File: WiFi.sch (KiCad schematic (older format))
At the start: 17 parts, among them J4 USB_B_Micro, J5 ESP_01, Q2 Q_NPN_EBC, Q3 Q_NPN_EBC, U8 CP2102N-A01-GQFN28, U9 TS5A3167DBVR

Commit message: Minor changes in pinout and layout
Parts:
- U8: symbol Interface_USB:CP2102N-A01-GQFN28 -> synermycha-electronics-rescue:CP2102N-A01-GQFN28-Interface_USB
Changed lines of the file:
@@
 $EndComp
 $Comp
-L Interface_USB:CP2102N-A01-GQFN28 U8
+L synermycha-electronics-rescue:CP2102N-A01-GQFN28-Interface_USB U8
 U 1 1 5E702C74
 P 4300 5200

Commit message: Minor update in pin connections
Connected Mouse eye led to PWM output
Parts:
- removed Q2, Q3: Q_NPN_EBC, Package_TO_SOT_SMD:SOT-23, symbol Device:Q_NPN_EBC
- added Q2, Q3: BC847, Package_TO_SOT_SMD:SOT-23, symbol Transistor_BJT:BC847
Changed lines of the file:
@@
-$EndComp
-$Comp
-L Device:Q_NPN_EBC Q2
-U 1 1 5E70ECD5
-P 5550 4500
-AR Path="/5E5F55AD/5E70ECD5" Ref="Q2"  Part="1"
-AR Path="/5E79B5DD/5E70ECD5" Ref="Q?"  Part="1"
-F 0 "Q2" V 5400 4700 50  0000 C CNN
-F 1 "Q_NPN_EBC" V 5500 4850 50  0000 C CNN
-F 2 "Package_TO_SOT_SMD:SOT-23" H 5750 4600 50  0001 C CNN
-F 3 "~" H 5550 4500 50  0001 C CNN
-	1    5550 4500
-	0    1    1    0
-$EndComp
-$Comp
-L Device:Q_NPN_EBC Q3
-U 1 1 5E70FFDF
-P 5550 4850
-AR Path="/5E5F55AD/5E70FFDF" Ref="Q3"  Part="1"
-AR Path="/5E79B5DD/5E70FFDF" Ref="Q?"  Part="1"
-F 0 "Q3" V 5500 5050 50  0000 C CNN
-F 1 "Q_NPN_EBC" V 5400 5200 50  0000 C CNN
-F 2 "Package_TO_SOT_SMD:SOT-23" H 5750 4950 50  0001 C CNN
-F 3 "~" H 5550 4850 50  0001 C CNN
-	1    5550 4850
-	0    1    -1   0
 $EndComp
 $Comp
@@
 	8350 4500 8050 4500
 Connection ~ 8050 4500
+$Comp
+L Transistor_BJT:BC847 Q2
+U 1 1 5E7F7A4F
+P 5550 4500
+F 0 "Q2" V 5450 4700 50  0000 C CNN
+F 1 "BC847" V 5550 4750 50  0000 C CNN
+F 2 "Package_TO_SOT_SMD:SOT-23" H 5750 4425 50  0001 L CIN
+F 3 "http://www.infineon.com/dgdl/Infineon-BC847SERIES_BC848SERIES_BC849SERIES_BC850SERIES-DS-v01_01-en.pdf?fileId=db3a304314dca389011541d4630a1657" H 5550 4500 50  0001 L CNN
+	1    5550 4500
+	0    1    1    0
+$EndComp
+$Comp
+L Transistor_BJT:BC847 Q3
+U 1 1 5E7F94B2
+P 5550 4850
+F 0 "Q3" V 5500 5050 50  0000 C CNN
+F 1 "BC847" V 5400 5100 50  0000 C CNN
+F 2 "Package_TO_SOT_SMD:SOT-23" H 5750 4775 50  0001 L CIN
+F 3 "http://www.infineon.com/dgdl/Infineon-BC847SERIES_BC848SERIES_BC849SERIES_BC850SERIES-DS-v01_01-en.pdf?fileId=db3a304314dca389011541d4630a1657" H 5550 4850 50  0001 L CNN
+	1    5550 4850
+	0    1    -1   0
+$EndComp
 $EndSCHEMATC

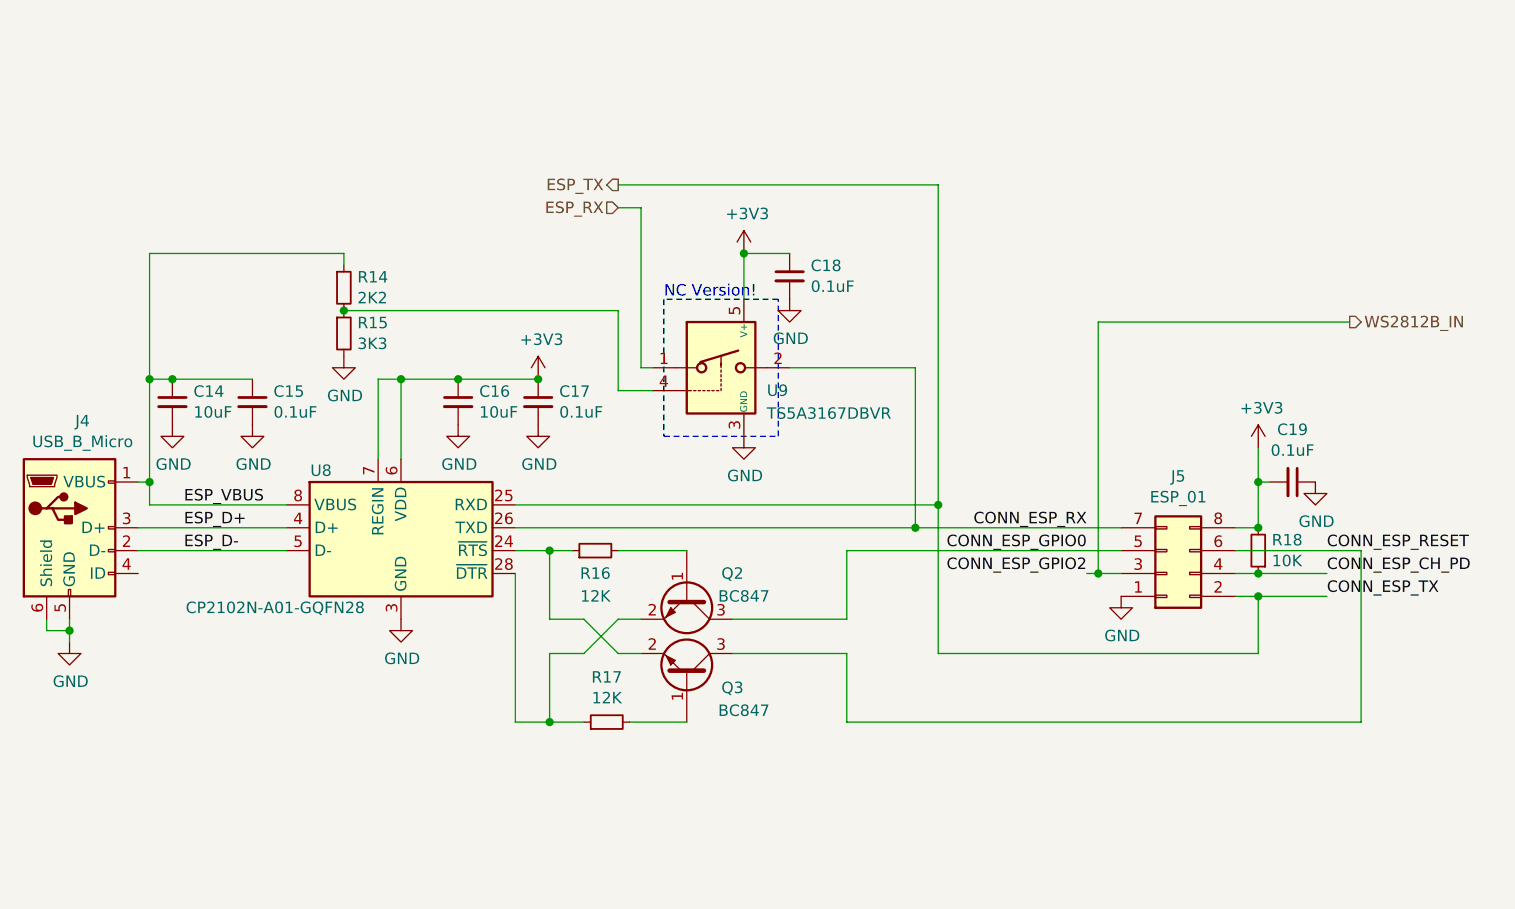
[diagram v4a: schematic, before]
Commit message: Czyszczenie
Usunięto linie 5V oraz 2V8. Poprawiono symbol dla diody RGB
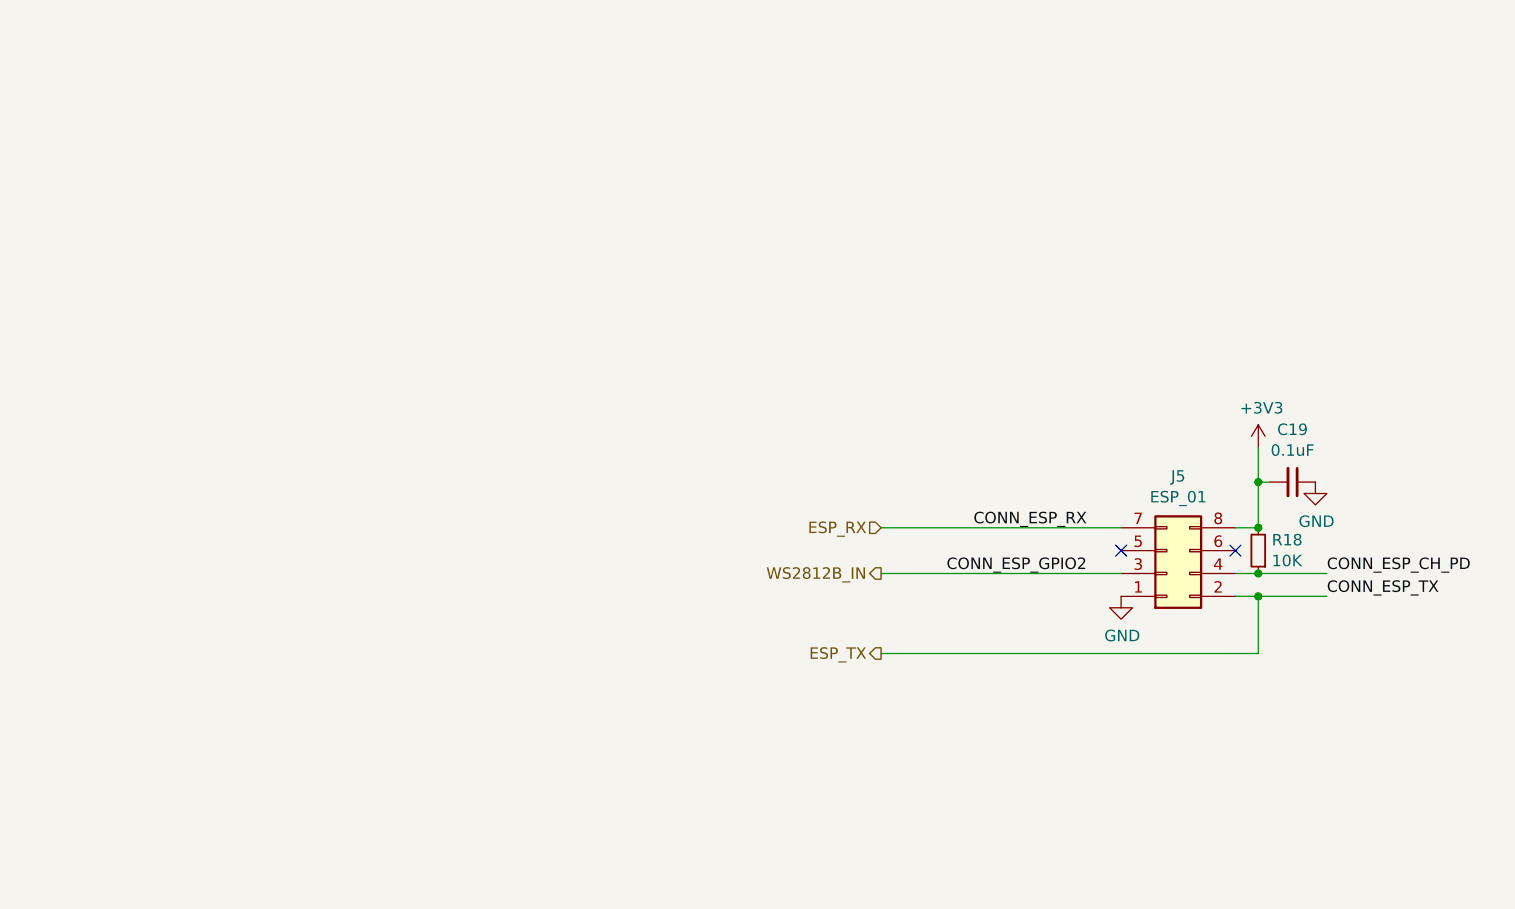
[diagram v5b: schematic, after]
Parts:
- removed C14, C16: 10uF, Capacitor_SMD:C_0603_1608Metric, symbol Device:C_Small
- removed C15, C17, C18: 0.1uF, Capacitor_SMD:C_0402_1005Metric, symbol Device:C_Small
- removed J4: USB_B_Micro, Connector_USB:USB_Micro-B_Amphenol_10103594-0001LF_Horizontal, symbol Connector:USB_B_Micro
- removed Q2, Q3: BC847, Package_TO_SOT_SMD:SOT-23, symbol Transistor_BJT:BC847
- removed R14: 2K2, Resistor_SMD:R_0402_1005Metric, symbol Device:R_Small
- removed R15: 3K3, Resistor_SMD:R_0402_1005Metric, symbol Device:R_Small
- removed R16, R17: 12K, Resistor_SMD:R_0402_1005Metric, symbol Device:R_Small
- removed U8: CP2102N-A01-GQFN28, Package_DFN_QFN:QFN-28-1EP_5x5mm_P0.5mm_EP3.35x3.35mm, symbol synermycha-electronics-rescue:CP2102N-A01-GQFN28-Interface_USB
- removed U9: TS5A3167DBVR, Package_TO_SOT_SMD:SOT-23-5, symbol Analog_Switch:TS5A3166DBVR
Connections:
- net CONN_ESP_RX is gone; now on net ESP_RX: J5.7 (Pin_7)
- net CONN_ESP_GPIO0: no longer names the net of J5.5 (Pin_5)
- net CONN_ESP_RESET: no longer names the net of J5.6 (Pin_6)
- no-connect marks 0 -> 2
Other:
- note removed: "NC Version!"

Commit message: Zmieniono moduł wifi na bluetooth oraz złącze usb - c
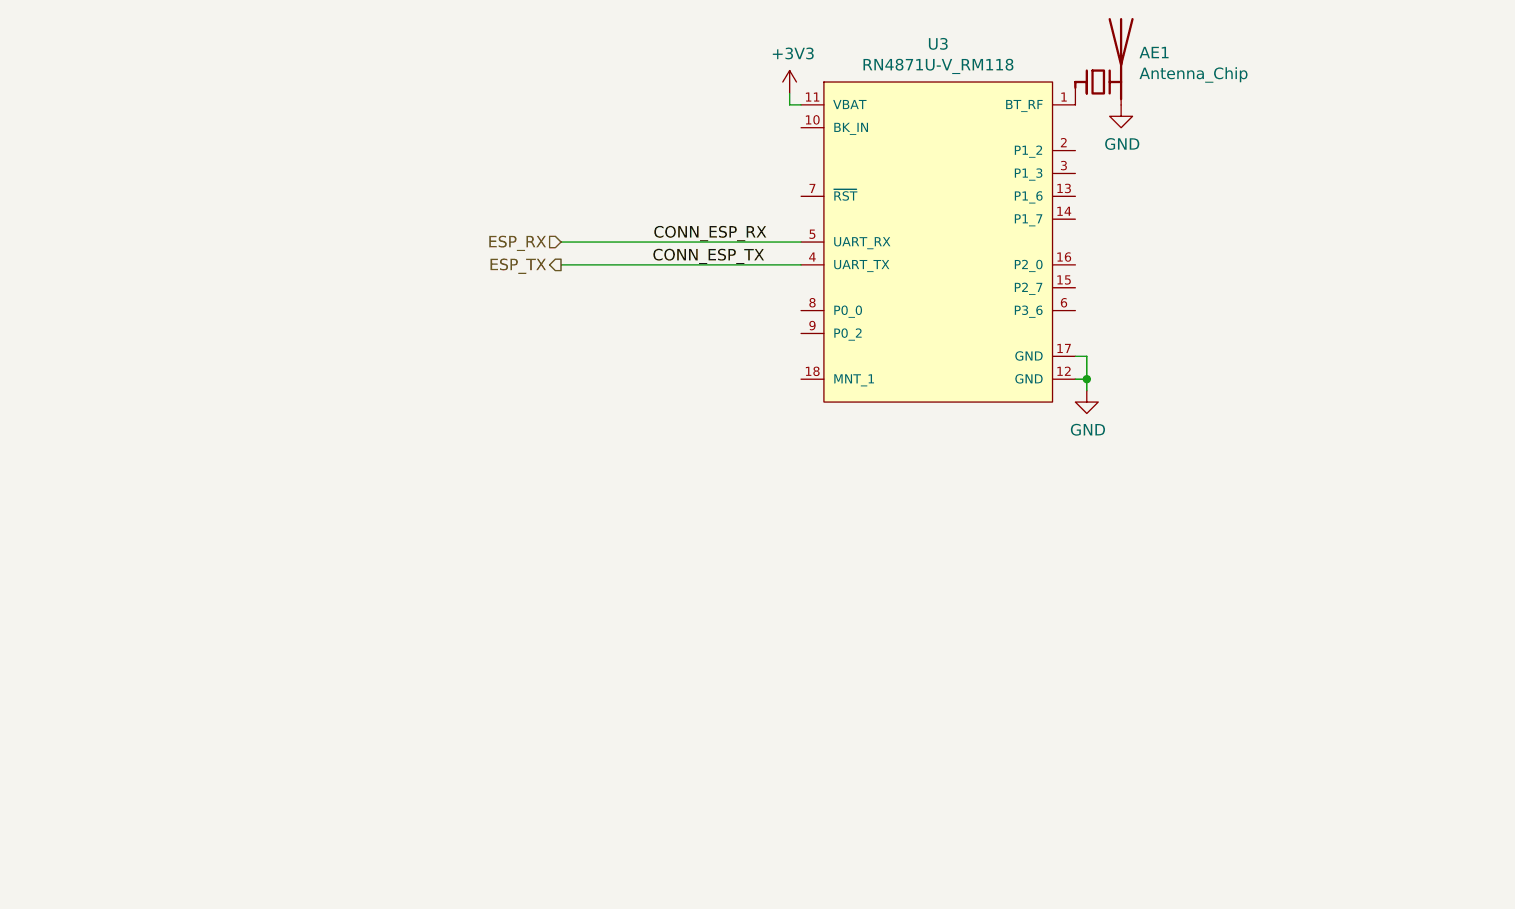
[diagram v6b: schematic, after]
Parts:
- removed C19: 0.1uF, Capacitor_SMD:C_0402_1005Metric, symbol Device:C_Small
- removed J5: ESP_01, Connector_PinSocket_2.54mm:PinSocket_2x04_P2.54mm_Vertical_SMD, symbol Connector_Generic:Conn_02x04_Odd_Even
- removed R18: 10K, Resistor_SMD:R_0402_1005Metric, symbol Device:R_Small
- added AE1: Antenna_Chip, RF_Antenna:Johanson_2450AT18x100, symbol Device:Antenna_Chip
- added U3: RN4871U-V_RM118, eec:Microchip-RN4871U-V_RM118-0, symbol eec:RN4871U-V_RM118
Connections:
- net +3V3: now also U3.11 (VBAT)
- net ESP_RX: now also U3.5 (UART_RX)
- net ESP_TX: now also U3.4 (UART_TX)
- net GND: now also AE1.2 (PCB_Trace), U3.12 (GND), U3.17 (GND)
- new net: AE1.1 (FEED), U3.1 (BT_RF)
- no-connect marks 2 -> 0
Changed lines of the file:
@@
 Comment4 ""
 $EndDescr
-Text HLabel 6400 4200 0    50   Input ~ 0
+Text HLabel 5000 2950 0    50   Input ~ 0
 ESP_RX
-Text HLabel 6400 4750 0    50   Output ~ 0
+Text HLabel 5000 3050 0    50   Output ~ 0
 ESP_TX
-Text HLabel 6400 4400 0    50   Output ~ 0
-WS2812B_IN
-Wire Wire Line
-	8050 4000 8050 4200
-Connection ~ 8050 4000
-Wire Wire Line
-	8100 4000 8050 4000
-Wire Wire Line
-	8050 3850 8050 4000
-Connection ~ 8050 4200
-Wire Wire Line
-	8050 4400 7950 4400
-$Comp
-L Device:R_Small R18
-U 1 1 5E7AA223
-P 8050 4300
-F 0 "R18" H 7991 4254 50  0000 R CNN
-F 1 "10K" H 7991 4345 50  0000 R CNN
-F 2 "Resistor_SMD:R_0402_1005Metric" H 8050 4300 50  0001 C CNN
-F 3 "~" H 8050 4300 50  0001 C CNN
-	1    8050 4300
-	-1   0    0    1
-$EndComp
-Wire Wire Line
-	8050 4500 7950 4500
-Wire Wire Line
-	8050 4750 8050 4500
-Wire Wire Line
-	7950 4200 8050 4200
-$Comp
-L power:GND #PWR0145
-U 1 1 5E76CA12
-P 8300 4000
-AR Path="/5E5F55AD/5E76CA12" Ref="#PWR0145"  Part="1"
-AR Path="/5E79B5DD/5E76CA12" Ref="#PWR?"  Part="1"
-F 0 "#PWR0145" H 8300 3750 50  0001 C CNN
-F 1 "GND" H 8305 3827 50  0000 C CNN
-F 2 "" H 8300 4000 50  0001 C CNN
-F 3 "" H 8300 4000 50  0001 C CNN
-	1    8300 4000
-	1    0    0    -1
-$EndComp
 $Comp
 L power:+3V3 #PWR0146
 U 1 1 5E76CA0A
-P 8050 3850
+P 6000 2300
 AR Path="/5E5F55AD/5E76CA0A" Ref="#PWR0146"  Part="1"
 AR Path="/5E79B5DD/5E76CA0A" Ref="#PWR?"  Part="1"
-F 0 "#PWR0146" H 8050 3700 50  0001 C CNN
-F 1 "+3V3" H 8065 4023 50  0000 C CNN
-F 2 "" H 8050 3850 50  0001 C CNN
-F 3 "" H 8050 3850 50  0001 C CNN
-	1    8050 3850
+F 0 "#PWR0146" H 6000 2150 50  0001 C CNN
+F 1 "+3V3" H 6015 2473 50  0000 C CNN
+F 2 "" H 6000 2300 50  0001 C CNN
+F 3 "" H 6000 2300 50  0001 C CNN
+	1    6000 2300
 	1    0    0    -1
-$EndComp
-$Comp
-L Device:C_Small C19
-U 1 1 5E76CA04
-P 8200 4000
-AR Path="/5E5F55AD/5E76CA04" Ref="C19"  Part="1"
-AR Path="/5E79B5DD/5E76CA04" Ref="C?"  Part="1"
-F 0 "C19" V 7971 4000 50  0000 C CNN
-F 1 "0.1uF" V 8062 4000 50  0000 C CNN
-F 2 "Capacitor_SMD:C_0402_1005Metric" H 8200 4000 50  0001 C CNN
-F 3 "~" H 8200 4000 50  0001 C CNN
-	1    8200 4000
-	0    1    1    0
 $EndComp
 $Comp
 L power:GND #PWR0147
 U 1 1 5E76775C
-P 7450 4500
+P 7300 3600
 AR Path="/5E5F55AD/5E76775C" Ref="#PWR0147"  Part="1"
 AR Path="/5E79B5DD/5E76775C" Ref="#PWR?"  Part="1"
-F 0 "#PWR0147" H 7450 4250 50  0001 C CNN
-F 1 "GND" H 7455 4327 50  0000 C CNN
-F 2 "" H 7450 4500 50  0001 C CNN
-F 3 "" H 7450 4500 50  0001 C CNN
-	1    7450 4500
+F 0 "#PWR0147" H 7300 3350 50  0001 C CNN
+F 1 "GND" H 7305 3427 50  0000 C CNN
+F 2 "" H 7300 3600 50  0001 C CNN
+F 3 "" H 7300 3600 50  0001 C CNN
+	1    7300 3600
+	1    0    0    -1
+$EndComp
+Text Label 5900 2950 2    50   ~ 0
+CONN_ESP_RX
+Text Label 5400 3050 0    50   ~ 0
+CONN_ESP_TX
+Wire Wire Line
+	5000 2950 6050 2950
+$Comp
+L eec:RN4871U-V_RM118 U3
+U 1 1 5F776A6D
+P 5950 2350
+F 0 "U3" H 6650 2615 50  0000 C CNN
+F 1 "RN4871U-V_RM118" H 6650 2524 50  0000 C CNN
+F 2 "eec:Microchip-RN4871U-V_RM118-0" H 5950 2750 50  0001 L CNN
+F 3 "http://ww1.microchip.com/downloads/en/DeviceDoc/50002489C.pdf" H 5950 2850 50  0001 L CNN
+F 4 "IC" H 5950 2950 50  0001 L CNN "category"
+F 5 "BLUETOOTH 4.2 BLE MODULE, UNSHIE" H 5950 3050 50  0001 L CNN "digikey description"
+F 6 "RN4871U-V/RM118-ND" H 5950 3150 50  0001 L CNN "digikey part number"
+F 7 "yes" H 5950 3250 50  0001 L CNN "lead free"
+F 8 "836aeee1b1e3abae" H 5950 3350 50  0001 L CNN "library id"
+F 9 "Microchip" H 5950 3450 50  0001 L CNN "manufacturer"
+F 10 "579-RN4871U-V/RM118" H 5950 3550 50  0001 L CNN "mouser part number"
+F 11 "SMD17" H 5950 3650 50  0001 L CNN "package"
+F 12 "yes" H 5950 3750 50  0001 L CNN "rohs"
+F 13 "+70°C" H 5950 3850 50  0001 L CNN "temperature range high"
+F 14 "-20°C" H 5950 3950 50  0001 L CNN "temperature range low"
+	1    5950 2350
+	1    0    0    -1
+$EndComp
+Wire Wire Line
+	6050 3050 5000 3050
+Wire Wire Line
+	7250 3450 7300 3450
+Wire Wire Line
+	7300 3450 7300 3550
+Wire Wire Line
+	7250 3550 7300 3550
+Connection ~ 7300 3550
+Wire Wire Line
+	7300 3550 7300 3600
+Wire Wire Line
+	6050 2350 6000 2350
+Wire Wire Line
+	6000 2350 6000 2300
+$Comp
+L Device:Antenna_Chip AE1
+U 1 1 5F7823BD
+P 7350 2250
+F 0 "AE1" H 7530 2377 50  0000 L CNN
+F 1 "Antenna_Chip" H 7530 2286 50  0000 L CNN
+F 2 "RF_Antenna:Johanson_2450AT18x100" H 7250 2425 50  0001 C CNN
+F 3 "~" H 7250 2425 50  0001 C CNN
+	1    7350 2250
 	1    0    0    -1
 $EndComp
 $Comp
-L Connector_Generic:Conn_02x04_Odd_Even J5
-U 1 1 5E762F6E
-P 7650 4400
-AR Path="/5E5F55AD/5E762F6E" Ref="J5"  Part="1"
-AR Path="/5E79B5DD/5E762F6E" Ref="J?"  Part="1"
-F 0 "J5" H 7700 3975 50  0000 C CNN
-F 1 "ESP_01" H 7700 4066 50  0000 C CNN
-F 2 "Connector_PinSocket_2.54mm:PinSocket_2x04_P2.54mm_Vertical_SMD" H 7650 4400 50  0001 C CNN
-F 3 "~" H 7650 4400 50  0001 C CNN
-	1    7650 4400
-	1    0    0    1
+L power:GND #PWR0145
+U 1 1 5F782DB6
+P 7450 2350
+AR Path="/5E5F55AD/5F782DB6" Ref="#PWR0145"  Part="1"
+AR Path="/5E79B5DD/5F782DB6" Ref="#PWR?"  Part="1"
+F 0 "#PWR0145" H 7450 2100 50  0001 C CNN
+F 1 "GND" H 7455 2177 50  0000 C CNN
+F 2 "" H 7450 2350 50  0001 C CNN
+F 3 "" H 7450 2350 50  0001 C CNN
+	1    7450 2350
+	1    0    0    -1
 $EndComp
-Text Label 7300 4200 2    50   ~ 0
-CONN_ESP_RX
-Text Label 7300 4400 2    50   ~ 0
-CONN_ESP_GPIO2
-Text Label 8350 4500 0    50   ~ 0
-CONN_ESP_TX
-Text Label 8350 4400 0    50   ~ 0
-CONN_ESP_CH_PD
-Wire Wire Line
-	8350 4400 8050 4400
-Connection ~ 8050 4400
-Wire Wire Line
-	8350 4500 8050 4500
-Connection ~ 8050 4500
-Wire Wire Line
-	6400 4750 8050 4750
-Wire Wire Line
-	6400 4200 7450 4200
-Wire Wire Line
-	6400 4400 7450 4400
-NoConn ~ 7450 4300
-NoConn ~ 7950 4300
 $EndSCHEMATC
